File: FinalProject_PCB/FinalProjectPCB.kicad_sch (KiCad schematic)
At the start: 13 parts, among them J1 SerialJack, SW1 SW_Push_Dual, SW2 SW_Push_Dual, SW3 SW_Push_Dual, SW4 SW_Push_Dual, SW5 SW_Push_Dual, SW6 SW_Push_Dual, SW7 SW_SPST, U1 ESP32-S2-DevKitC-1

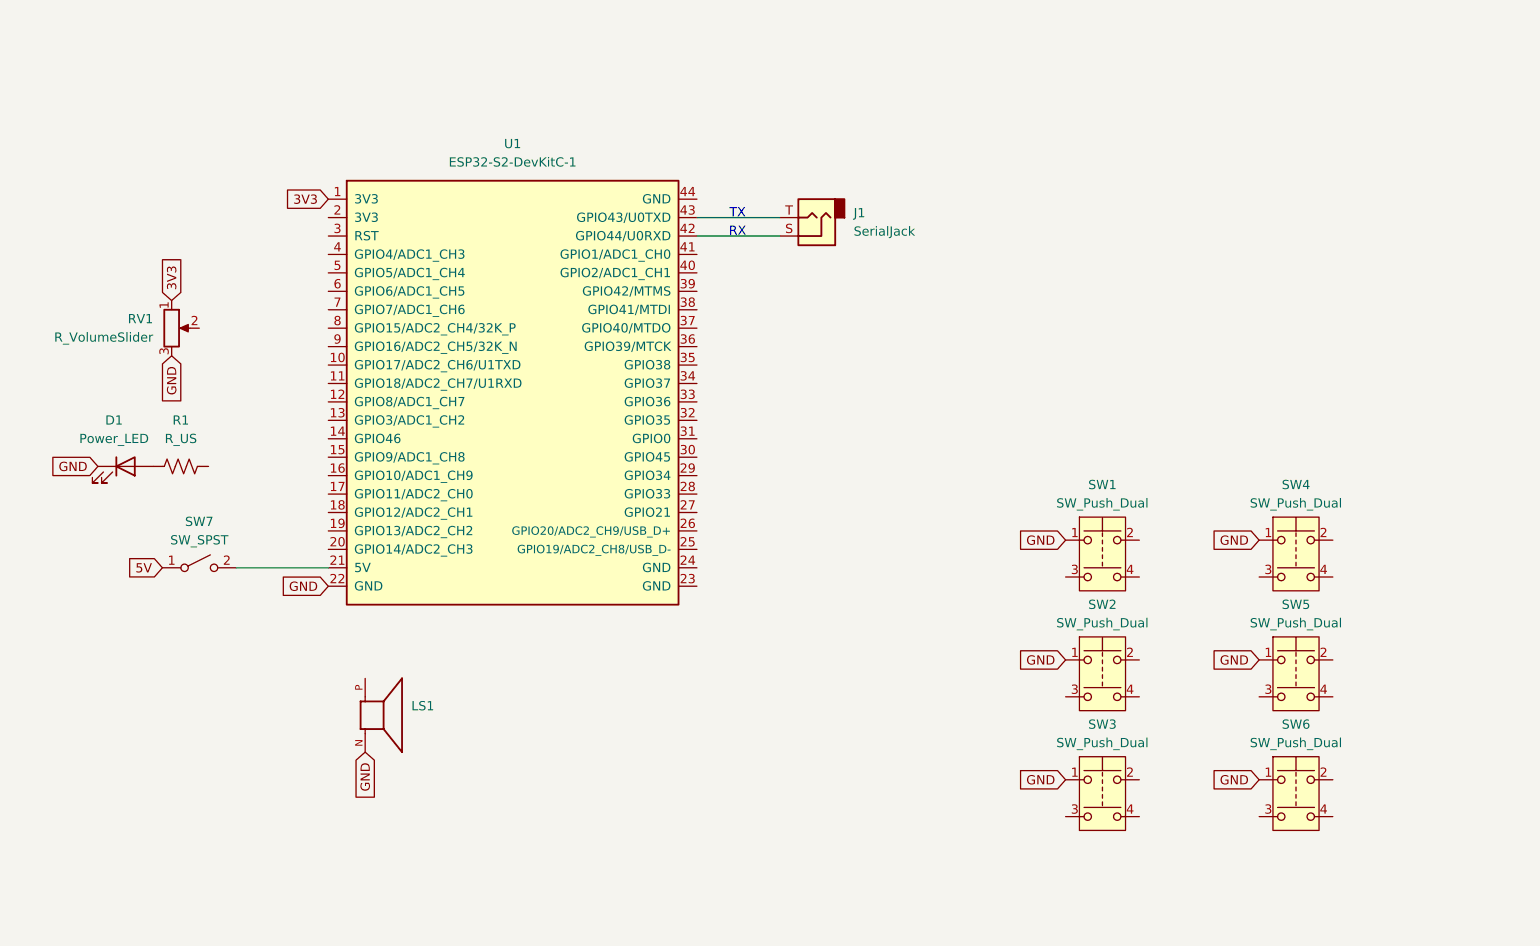
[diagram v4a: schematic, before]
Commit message: tagged all components
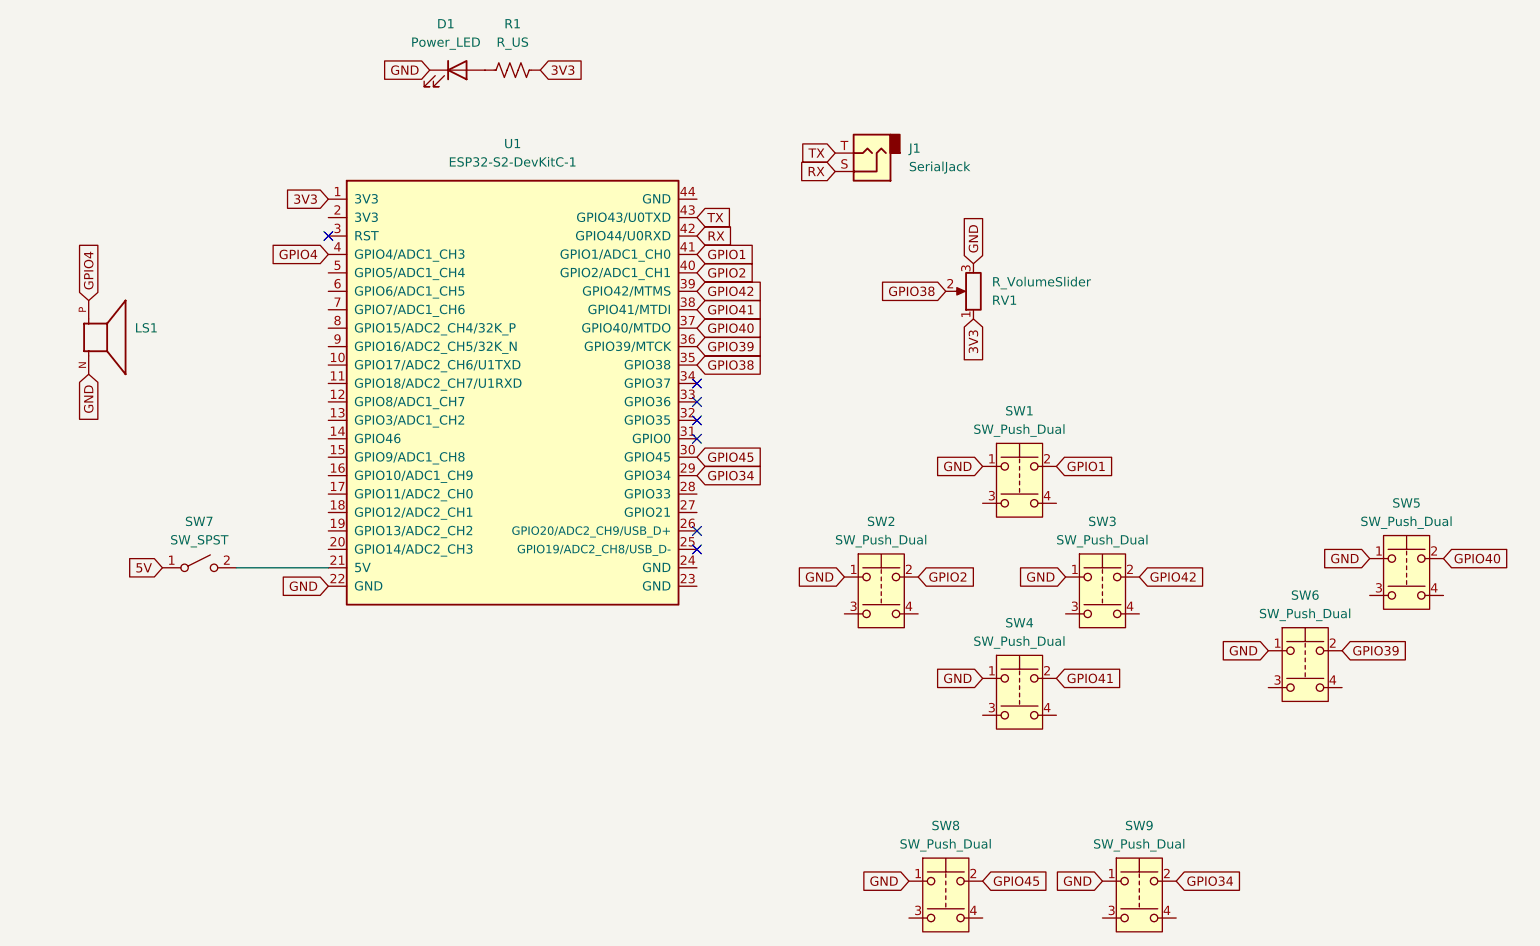
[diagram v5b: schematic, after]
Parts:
- added SW8, SW9: SW_Push_Dual, symbol Switch:SW_Push_Dual
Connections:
- net 3V3: now also R1.2
- net GND: now also SW8.1, SW9.1
- net GPIO1: now reaches SW1.2
- net GPIO1: now also U1.41 (GPIO1/ADC1_CH0)
- net GPIO40: now reaches SW5.2
- net GPIO40: now also U1.37 (GPIO40/MTDO)
- net GPIO34: now reaches U1.29 (GPIO34)
- net GPIO34: now also SW9.2
- net GPIO45: now reaches U1.30 (GPIO45)
- net GPIO45: now also SW8.2
- net GPIO38: now reaches U1.35 (GPIO38)
- net GPIO38: now also RV1.2
- net GPIO39: now reaches U1.36 (GPIO39/MTCK)
- net GPIO39: now also SW6.2
- net GPIO41: now reaches U1.38 (GPIO41/MTDI)
- net GPIO41: now also SW4.2
- net GPIO42: now reaches U1.39 (GPIO42/MTMS)
- net GPIO42: now also SW3.2
- net GPIO4: now reaches U1.4 (GPIO4/ADC1_CH3)
- net GPIO4: now also LS1.P
- net GPIO2: now reaches U1.40 (GPIO2/ADC1_CH1)
- net GPIO2: now also SW2.2
- net RX: now reaches J1.S, U1.42 (GPIO44/U0RXD)
- net TX: now reaches J1.T, U1.43 (GPIO43/U0TXD)
- no-connect marks 0 -> 7
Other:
- note removed: "RX"
- note removed: "TX"
- moved on the sheet: D1, J1, LS1, R1, RV1, SW1, SW2, SW3, SW4, SW5, SW6

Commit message: fixed button wiring
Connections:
- net GPIO1: now also SW1.4; no longer SW1.2
- net GPIO2: now also SW2.4; no longer SW2.2
- net GPIO34: now also SW9.4; no longer SW9.2
- net GPIO39: now also SW6.4; no longer SW6.2
- net GPIO40: now also SW5.4; no longer SW5.2
- net GPIO41: now also SW4.4; no longer SW4.2
- net GPIO42: now also SW3.4; no longer SW3.2
- net GPIO45: now also SW8.4; no longer SW8.2

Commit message: added some footprints
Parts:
- added J2: Conn_01x09, symbol Connector_Generic:Conn_01x09
- D1: footprint (none) -> LED_THT:LED_D3.0mm
- LS1: footprint Piezo -> GooseCustom:Piezo_XDCR_AT-1224-TWT-5V-2-R
- SW1, SW2, SW3, SW4, SW5, SW6, SW8, SW9: footprint (none) -> Button_Switch_THT:SW_PUSH-12mm
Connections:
- net 3V3: now also J2.9 (Pin_9)
- net GND: now also J2.8 (Pin_8)
- no-connect marks 7 -> 23
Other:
- note added: "CS"
- note added: "DC/RS"
- note added: "GND"
- note added: "LED"
- note added: "RESET"
- note added: "SCK"
- note added: "SDD/MISO"
- note added: "SDI/MOSI"
- note added: "VCC -3v3/5V"

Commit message: added backlight options
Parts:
- added JP1, JP2: Jumper_2_Open, symbol Jumper:Jumper_2_Open
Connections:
- net 3V3: now also JP1.1 (A)
- net GPIO17: now reaches U1.10 (GPIO17/ADC2_CH6/U1TXD)
- net GPIO17: now also J2.6 (Pin_6)
- net GPIO18: now reaches U1.11 (GPIO18/ADC2_CH7/U1RXD)
- net GPIO18: now also J2.7 (Pin_7)
- net GPIO5: now reaches U1.5 (GPIO5/ADC1_CH4)
- net GPIO5: now also J2.1 (Pin_1)
- net GPIO6: now reaches U1.6 (GPIO6/ADC1_CH5)
- net GPIO6: now also JP2.1 (A)
- net GPIO7: now reaches U1.7 (GPIO7/ADC1_CH6)
- net GPIO7: now also J2.3 (Pin_3)
- net GPIO15: now reaches U1.8 (GPIO15/ADC2_CH4/32K_P)
- net GPIO15: now also J2.4 (Pin_4)
- net GPIO16: now reaches U1.9 (GPIO16/ADC2_CH5/32K_N)
- net GPIO16: now also J2.5 (Pin_5)
- net at J2.2 (Pin_2): now also JP1.2 (B), JP2.2 (B)
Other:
- note added: "Pick One"
